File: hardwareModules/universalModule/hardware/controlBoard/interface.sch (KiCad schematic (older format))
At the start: 9 parts, among them J2 OLED_DISPLAY, SW1 SW_Push, SW2 STOP_BUTTON, SW3 SW_Push, SW4 START_BUTTON, SW5 SW_Push

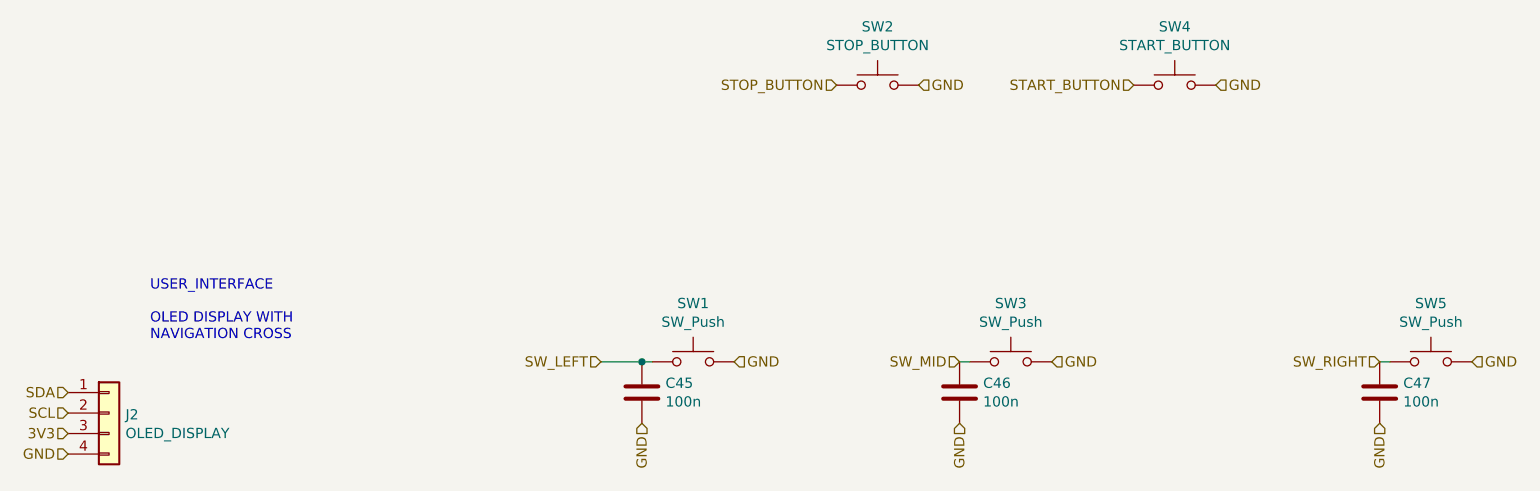
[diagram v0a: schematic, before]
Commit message: universalModule: Draft schematics of the new version of the control board
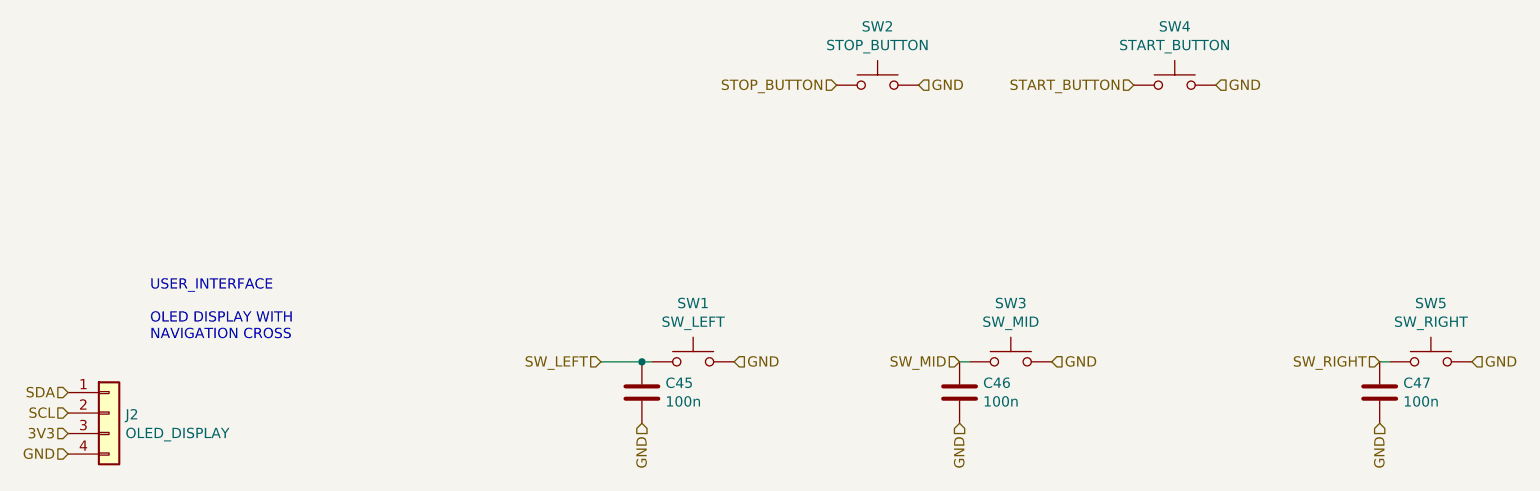
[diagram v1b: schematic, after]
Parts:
- SW1: value SW_Push -> SW_LEFT; LCSC (none) -> C2681478
- SW2, SW4: LCSC (none) -> C2681478
- SW3: value SW_Push -> SW_MID; LCSC (none) -> C2681478
- SW5: value SW_Push -> SW_RIGHT; LCSC (none) -> C2681478
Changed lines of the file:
@@
 $Descr A4 11693 8268
 encoding utf-8
-Sheet 5 6
+Sheet 4 5
 Title ""
 Date ""
@@
 AR Path="/5E8D0C73/5DEE098E" Ref="SW3"  Part="1"
 F 0 "SW3" H 7000 3835 50  0000 C CNN
-F 1 "SW_Push" H 7000 3744 50  0000 C CNN
+F 1 "SW_MID" H 7000 3744 50  0000 C CNN
 F 2 "rofi:BUTTON_SMT_G_4_3" H 7000 3750 50  0001 C CNN
 F 3 "~" H 7000 3750 50  0001 C CNN
 F 4 "PTS636 SL43 LFS" H 7000 3550 50  0001 C CNN "#manf"
+F 5 "C2681478" H 7000 3550 50  0001 C CNN "LCSC"
 	1    7000 3550
 	1    0    0    -1
@@
 AR Path="/5E8D0C73/5DEE0996" Ref="SW1"  Part="1"
 F 0 "SW1" H 5450 3835 50  0000 C CNN
-F 1 "SW_Push" H 5450 3744 50  0000 C CNN
+F 1 "SW_LEFT" H 5450 3744 50  0000 C CNN
 F 2 "rofi:BUTTON_SMT_G_4_3" H 5450 3750 50  0001 C CNN
 F 3 "~" H 5450 3750 50  0001 C CNN
 F 4 "PTS636 SL43 LFS" H 5450 3550 50  0001 C CNN "#manf"
+F 5 "C2681478" H 5450 3550 50  0001 C CNN "LCSC"
 	1    5450 3550
 	1    0    0    -1
@@
 AR Path="/5E8D0C73/5DEE099D" Ref="SW5"  Part="1"
 F 0 "SW5" H 9050 3835 50  0000 C CNN
-F 1 "SW_Push" H 9050 3744 50  0000 C CNN
+F 1 "SW_RIGHT" H 9050 3744 50  0000 C CNN
 F 2 "rofi:BUTTON_SMT_G_4_3" H 9050 3750 50  0001 C CNN
 F 3 "~" H 9050 3750 50  0001 C CNN
 F 4 "PTS636 SL43 LFS" H 9050 3550 50  0001 C CNN "#manf"
+F 5 "C2681478" H 9050 3550 50  0001 C CNN "LCSC"
 	1    9050 3550
 	1    0    0    -1
@@
 F 3 "~" H 7800 2400 50  0001 C CNN
 F 4 "PTS636 SL43 LFS" H 7800 2200 50  0001 C CNN "#manf"
+F 5 "C2681478" H 7800 2200 50  0001 C CNN "LCSC"
 	1    7800 2200
 	1    0    0    -1
@@
 F 3 "~" H 6350 2400 50  0001 C CNN
 F 4 "PTS636 SL43 LFS" H 6350 2200 50  0001 C CNN "#manf"
+F 5 "C2681478" H 6350 2200 50  0001 C CNN "LCSC"
 	1    6350 2200
 	1    0    0    -1

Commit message: universalModule: Prepare electronics v0.2
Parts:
- C45, C46, C47: LCSC (none) -> C1525
- J2: JLCPCB_IGNORE (none) -> YES
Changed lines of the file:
@@
 $Descr A4 11693 8268
 encoding utf-8
-Sheet 4 5
+Sheet 4 14
 Title ""
 Date ""
@@
 F 2 "rofi:OLED_128_32_I2C" H 2600 3800 50  0001 C CNN
 F 3 "~" H 2600 3800 50  0001 C CNN
+F 4 "YES" H 2600 3800 50  0001 C CNN "JLCPCB_IGNORE"
 	1    2600 3800
 	1    0    0    -1
@@
 F 3 "~" H 5200 3700 50  0001 C CNN
 F 4 "885012105016" H 5200 3700 50  0001 C CNN "#manf"
+F 5 "C1525" H 5200 3700 50  0001 C CNN "LCSC"
 	1    5200 3700
 	1    0    0    -1
@@
 F 3 "~" H 8800 3700 50  0001 C CNN
 F 4 "885012105016" H 8800 3700 50  0001 C CNN "#manf"
+F 5 "C1525" H 8800 3700 50  0001 C CNN "LCSC"
 	1    8800 3700
 	1    0    0    -1
@@
 F 3 "~" H 6750 3700 50  0001 C CNN
 F 4 "885012105016" H 6750 3700 50  0001 C CNN "#manf"
+F 5 "C1525" H 6750 3700 50  0001 C CNN "LCSC"
 	1    6750 3700
 	1    0    0    -1

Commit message: universalModule: Add final pre-production tweaks
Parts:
- SW1, SW2, SW3, SW4, SW5: LCSC C2681478 -> C520860
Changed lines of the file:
@@
 F 3 "~" H 7000 3750 50  0001 C CNN
 F 4 "PTS636 SL43 LFS" H 7000 3550 50  0001 C CNN "#manf"
-F 5 "C2681478" H 7000 3550 50  0001 C CNN "LCSC"
+F 5 "C520860" H 7000 3550 50  0001 C CNN "LCSC"
 	1    7000 3550
 	1    0    0    -1
@@
 F 3 "~" H 5450 3750 50  0001 C CNN
 F 4 "PTS636 SL43 LFS" H 5450 3550 50  0001 C CNN "#manf"
-F 5 "C2681478" H 5450 3550 50  0001 C CNN "LCSC"
+F 5 "C520860" H 5450 3550 50  0001 C CNN "LCSC"
 	1    5450 3550
 	1    0    0    -1
@@
 F 3 "~" H 9050 3750 50  0001 C CNN
 F 4 "PTS636 SL43 LFS" H 9050 3550 50  0001 C CNN "#manf"
-F 5 "C2681478" H 9050 3550 50  0001 C CNN "LCSC"
+F 5 "C520860" H 9050 3550 50  0001 C CNN "LCSC"
 	1    9050 3550
 	1    0    0    -1
@@
 F 3 "~" H 7800 2400 50  0001 C CNN
 F 4 "PTS636 SL43 LFS" H 7800 2200 50  0001 C CNN "#manf"
-F 5 "C2681478" H 7800 2200 50  0001 C CNN "LCSC"
+F 5 "C520860" H 7800 2200 50  0001 C CNN "LCSC"
 	1    7800 2200
 	1    0    0    -1
@@
 F 3 "~" H 6350 2400 50  0001 C CNN
 F 4 "PTS636 SL43 LFS" H 6350 2200 50  0001 C CNN "#manf"
-F 5 "C2681478" H 6350 2200 50  0001 C CNN "LCSC"
+F 5 "C520860" H 6350 2200 50  0001 C CNN "LCSC"
 	1    6350 2200
 	1    0    0    -1
